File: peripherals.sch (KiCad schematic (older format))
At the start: 29 parts, among them J10 CTC Header, J7 PIO Header, J8 Port B, J9 Port A, U7 Z84C2010AEG, U8 Z84C4310AEG, U9 Z84C3010AEG

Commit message: lots of fixes
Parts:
- added C4: 100nF, Capacitor_SMD:C_0603_1608Metric_Pad1.05x0.95mm_HandSolder, symbol Device:C_Small
- added D1: LED, LED_SMD:LED_0603_1608Metric_Pad1.05x0.95mm_HandSolder, symbol Device:LED
- added J4: IDE, Connector_PinHeader_2.54mm:PinHeader_2x20_P2.54mm_Horizontal, symbol Connector_Generic:Conn_02x20_Odd_Even
- added JP1: PWR, Connector_PinHeader_2.54mm:PinHeader_1x02_P2.54mm_Vertical, symbol Device:Jumper_NC_Small
- added R14: 1K, Resistor_SMD:R_0603_1608Metric_Pad1.05x0.95mm_HandSolder, symbol Device:R_Small
- added R6, R7, R8, R9: 10K, Resistor_SMD:R_0603_1608Metric_Pad1.05x0.95mm_HandSolder, symbol Device:R_Small
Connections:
- net labels added: A2, A[0..2], IDE_~CE, IEO_2, ~ACTIVE, ~RESET, ~WR
- net labels removed: A[0..1], IEO
- wire segments 188 -> 226
- no-connect marks 7 -> 20
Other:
- note added: "IDE/CF"
- moved on the sheet: C19, C20, C21, J7, J8, J9, JP2, JP3, R22, R23, R24, R25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

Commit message: fixed led values, added pwr led
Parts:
- D1: value LED -> Red
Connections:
- net labels added: CLK_7328
- net labels removed: CLK_U
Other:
- note added: "Mode 2 Interrupt Daisy Chain\n\nVCC (IEI) -> SIO -> IEO_0 -> \nPIO -> IEO_1 -> CTC -> IEO_2"
- moved on the sheet: C19, C20, C21, C4, D1, J4, JP1, R14, R6, R7, R8, R9

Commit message: fixes for CTC and additional clocks
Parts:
- removed J10: CTC Header, Connector_PinHeader_2.54mm:PinHeader_1x10_P2.54mm_Horizontal, symbol Connector_Generic:Conn_01x10
- removed R35, R36, R37, R38: 10K, Resistor_SMD:R_0603_1608Metric_Pad1.05x0.95mm_HandSolder, symbol THS-80-rescue:R_Small-Device-sbc_z80-rescue
- added J10: CT0, Connector_PinHeader_2.54mm:PinHeader_1x03_P2.54mm_Horizontal, symbol Connector_Generic:Conn_01x03
- added R35, R36: 10K, Resistor_SMD:R_0603_1608Metric_Pad1.05x0.95mm_HandSolder, symbol Device:R_Small
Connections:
- net labels removed: CLK_C, CT1, CT2
- wire segments 226 -> 200
- no-connect marks 20 -> 21
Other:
- moved on the sheet: U9

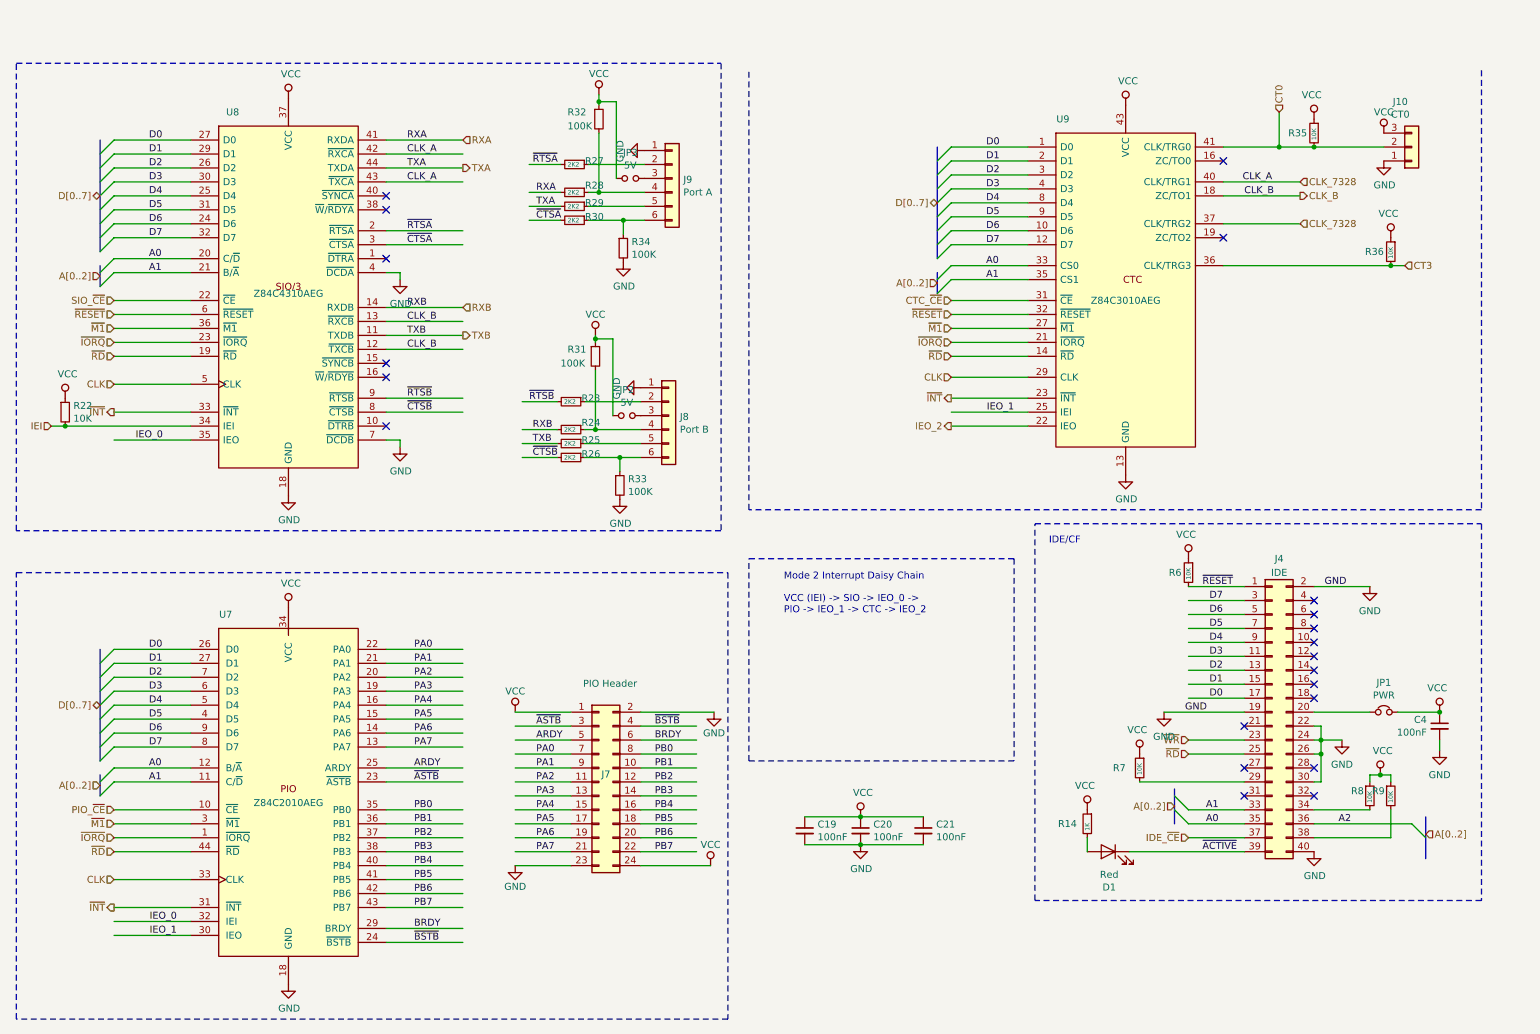
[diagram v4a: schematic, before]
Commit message: swapped CTC and PIO
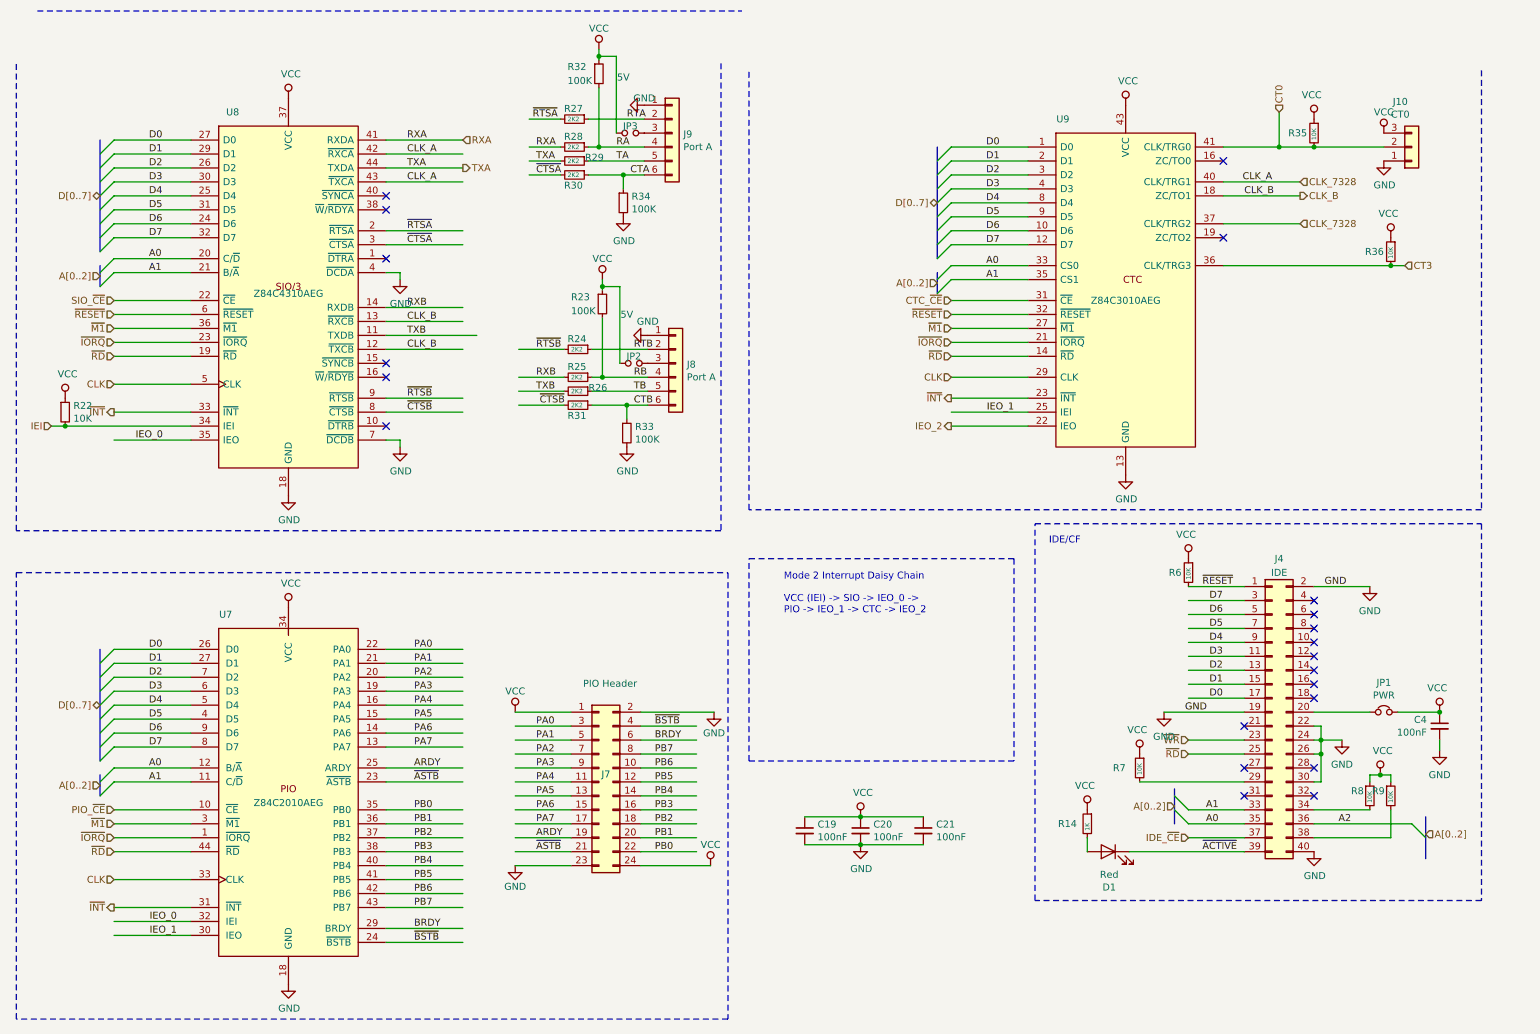
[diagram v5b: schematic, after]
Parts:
- J8: value Port B -> Port A
- R23: value 2K2 -> 100K
- R31: value 100K -> 2K2
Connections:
- net labels added: CTA, CTB, RA, RB, RTA, RTB, TA, TB
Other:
- moved on the sheet: J9, JP3, R27, R28, R29, R30, R32, R34

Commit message: lots of fixes
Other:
- moved on the sheet: J8, J9, JP2, JP3, R23, R24, R25, R26, R27, R28, R29, R30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

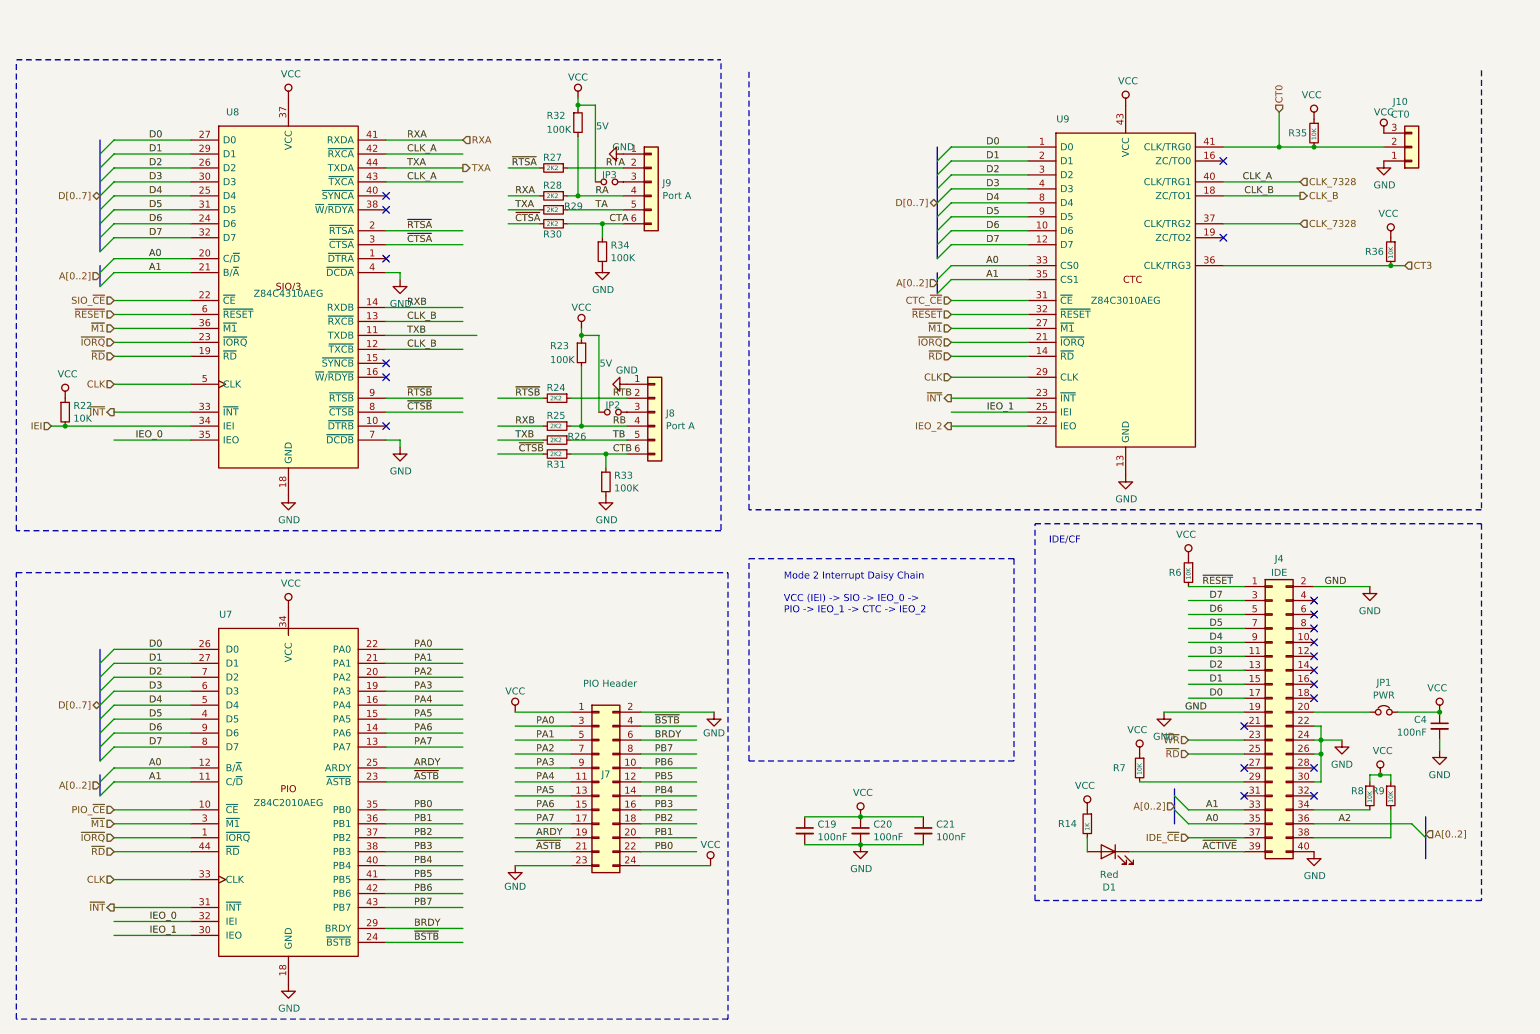
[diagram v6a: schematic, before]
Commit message: replaced VCC with 5V, fixed ROM footprint
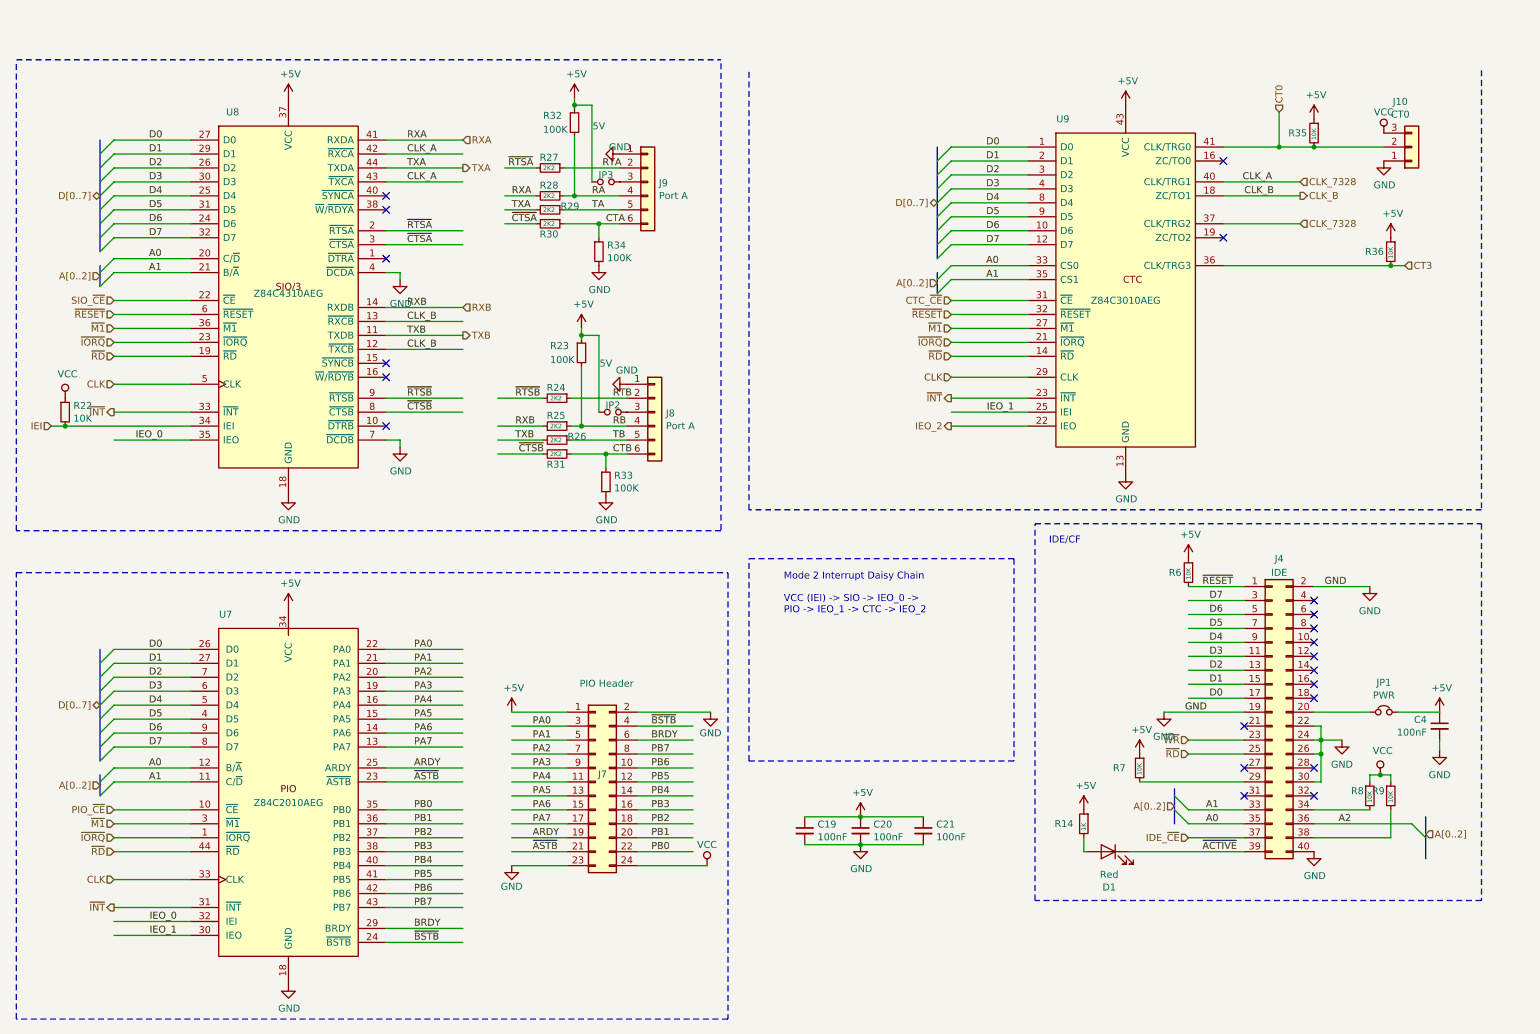
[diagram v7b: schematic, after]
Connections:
- net labels added: +5V
- wire segments 200 -> 201
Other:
- moved on the sheet: J7, J9, JP3, R14, R27, R28, R29, R30, R32, R34

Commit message: layout changes, silkscreen fixes
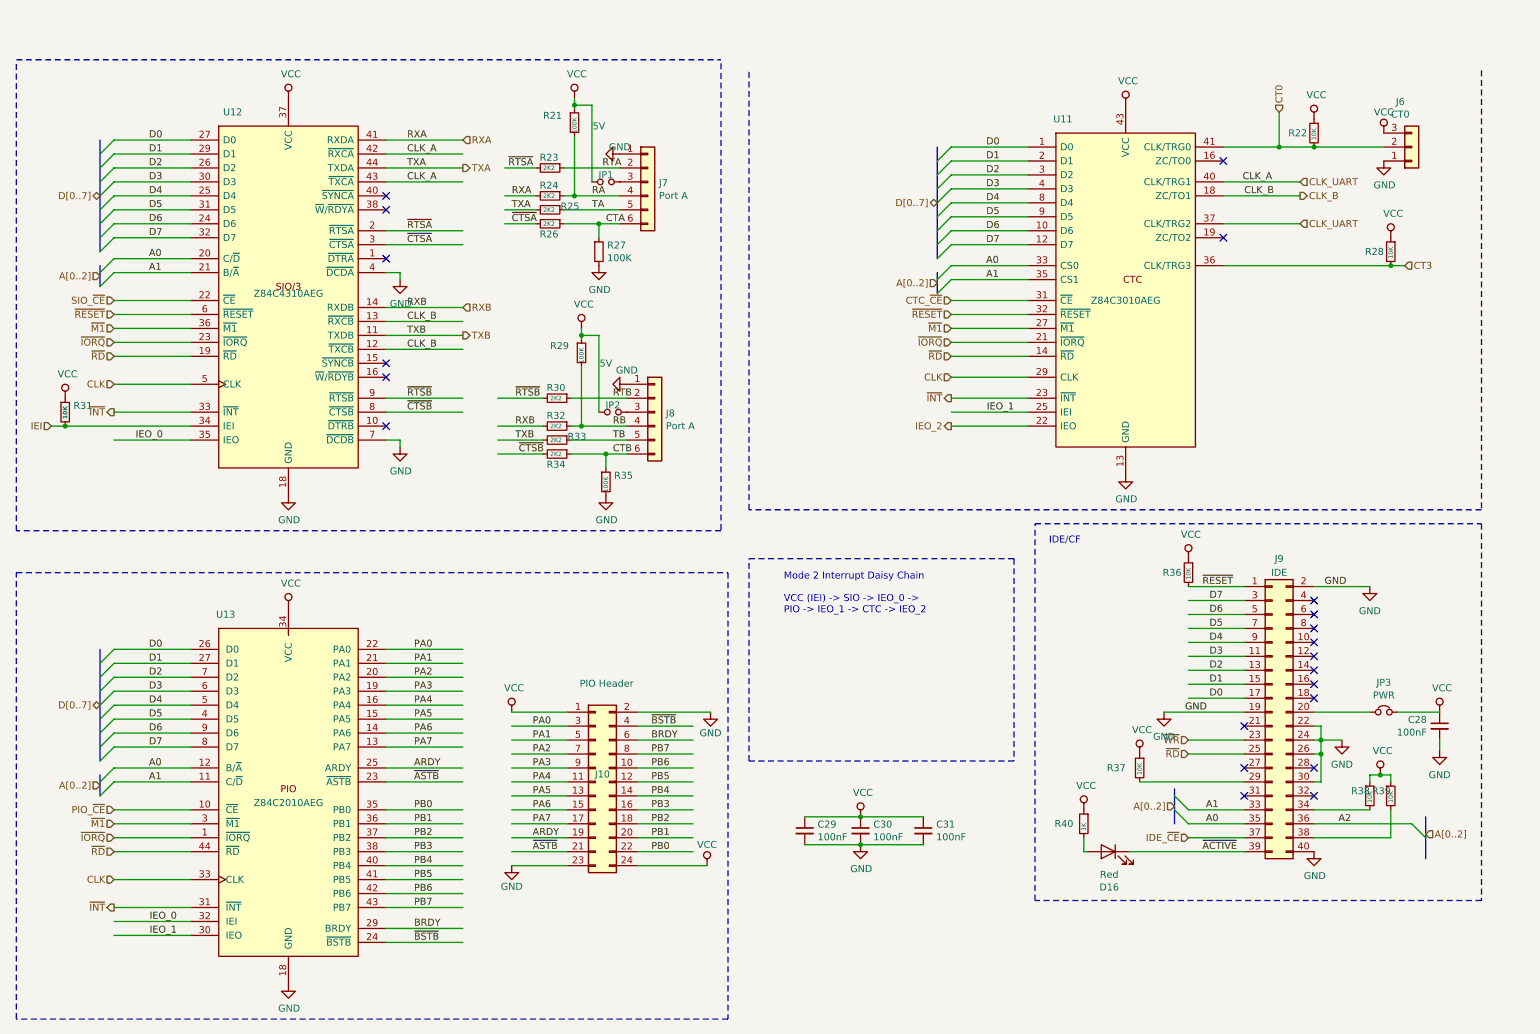
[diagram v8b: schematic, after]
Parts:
- renumbered C4 to C28, C19 to C29, C20 to C30, C21 to C31, D1 to D16, J7 to J10, J10 to J6, J9 to J7, J4 to J9, JP3 to JP1, JP1 to JP3, R32 to R21, R35 to R22, R27 to R23, R28 to R24, R29 to R25, R30 to R26, R34 to R27, R36 to R28, R23 to R29, R24 to R30, R22 to R31, R25 to R32, R26 to R33, R31 to R34, R33 to R35, R6 to R36, R7 to R37, R8 to R38, R9 to R39, R14 to R40, U9 to U11, U8 to U12, U7 to U13
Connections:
- net labels added: CLK_UART
- net labels removed: +5V, CLK_7328
